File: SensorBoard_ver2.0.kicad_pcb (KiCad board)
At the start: 2 copper layers, 82.5 x 50 mm, 55 parts, among them IC1 MIC5504-3.3YM5-T5, J1 CANConn, J13 Abso, J14 Abso, J15 STLink, J16 Abso, J18 Abso, J19 Abso, J2 CANConn, J20 Enc5, J3 Enc1, J4 Enc2, J5 Enc3, J6 Enc4, SW1 CAN_Terminal, SW2 IDSetSW, SW3 Reset, SW4 IDSetSW, U1 L7805, U2 ATA6561, U4 STM32F303K8Tx, U5 MAX3485, Y1 Crystal

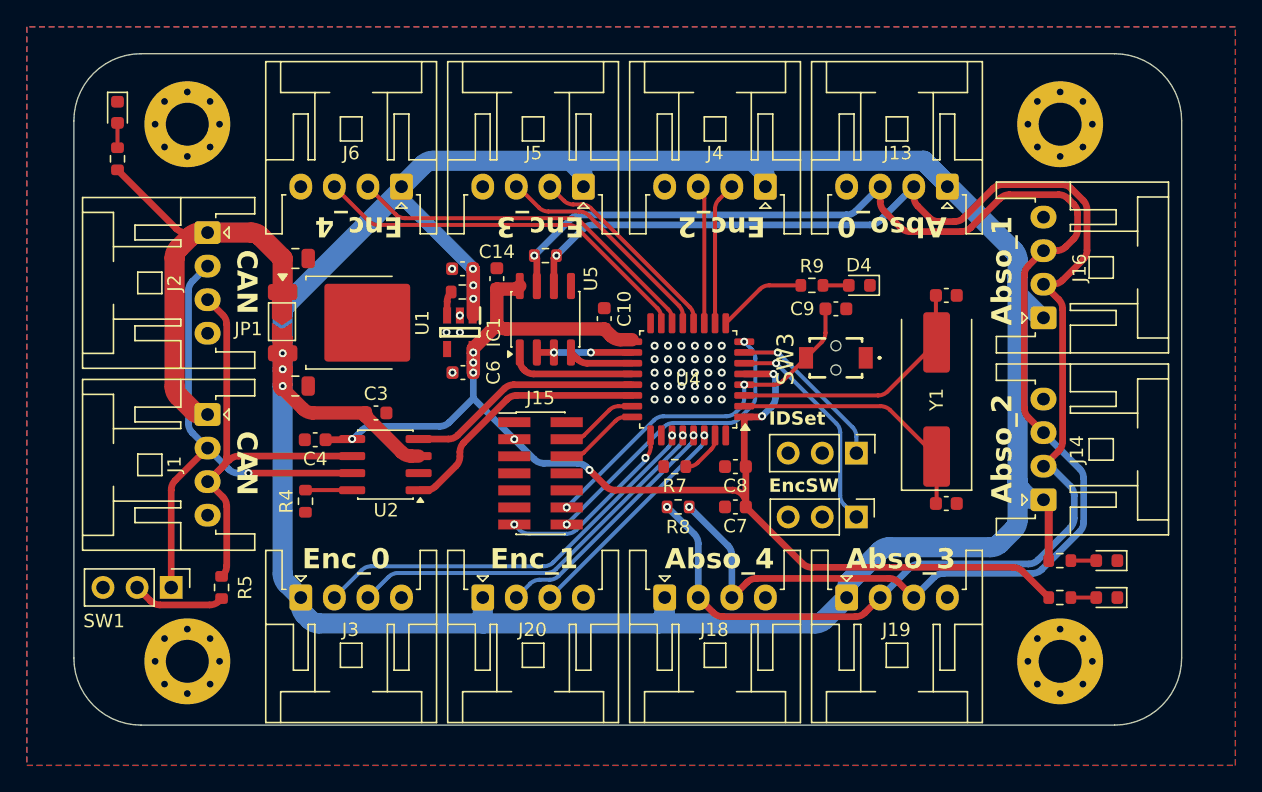
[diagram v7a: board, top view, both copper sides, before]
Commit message: ver1、完成形
なんか、いろいろ制御との兼ね合いでダメなところが出てきた…
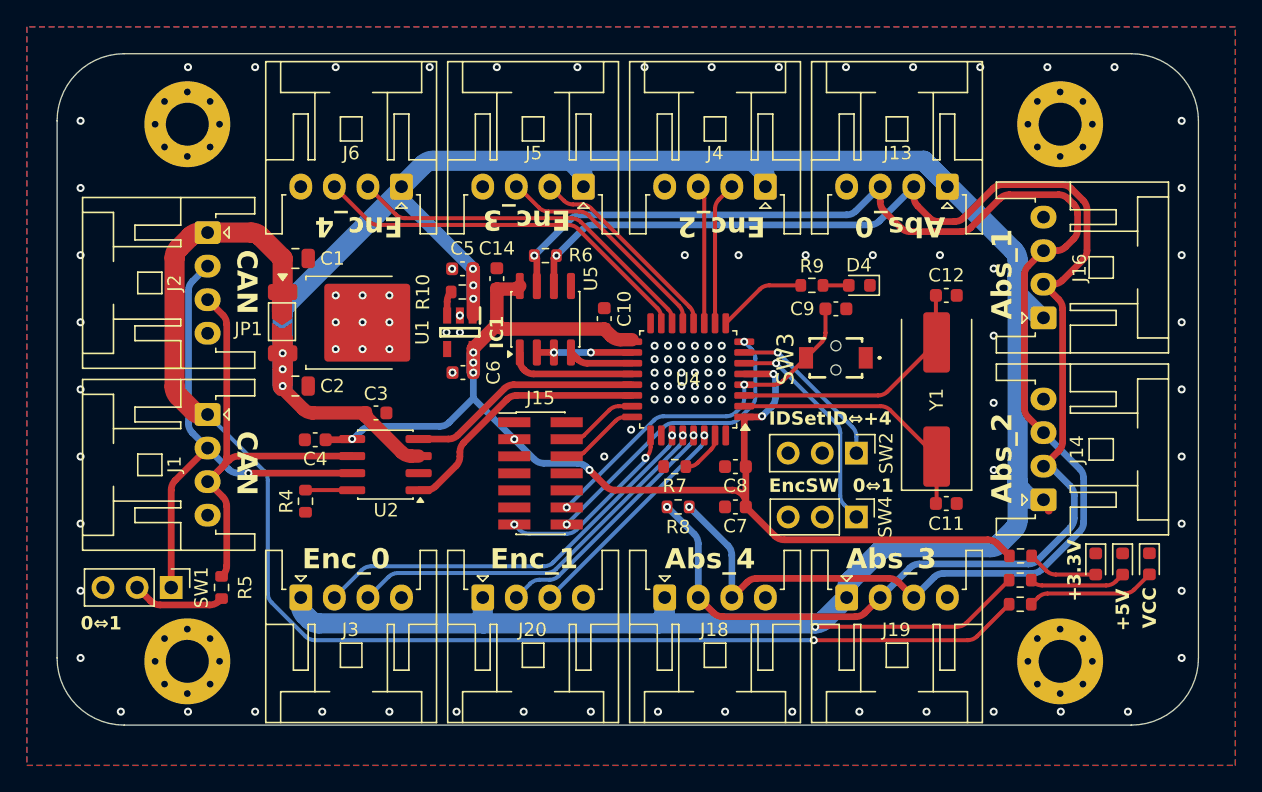
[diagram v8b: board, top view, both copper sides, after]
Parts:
- moved D1 83.9 mm to (138.6, 135.0)
- moved R1 75.0 mm to (129.0, 138.0), turned to 0 degrees
- moved R3 4.26 mm to (129.0, 134.4)
- moved R2 3.29 mm to (129.0, 136.2)
- moved D3 2.63 mm to (134.6, 135.0), turned to -90 degrees
- moved D2 1.20 mm to (136.6, 135.0), turned to -90 degrees
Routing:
- net VCC: track 35.4 -> 101.4 mm, vias 0 -> 1
- net Net-(D1-A): track 1.85 -> 9.63 mm
- net Net-(D2-A): track 1.89 -> 7.21 mm
- net +3.3V: track 97.6 -> 93.4 mm
- net +5V: track 214.3 -> 210.2 mm, vias 6 -> 7
- net Net-(D3-A): track 1.89 -> 5.30 mm
- net GND: vias 35 -> 103
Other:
- board size 82.5 x 50 mm -> 85 x 50 mm
- board text added: "+3.3V"
- board text added: "+5V"
- board text added: "0⇔1"
- board text added: "Abs_0"
- board text added: "Abs_1"
- board text added: "Abs_2"
- board text added: "Abs_3"
- board text added: "Abs_4"
- board text added: "ID⇔+4"
- board text added: "SensorBoard ver1"
- board text added: "VCC"
- board text added: "♨"
- board text added: "「Design」 Hardware:Hama Firmware:JAGA"
- board text added: "「Size」 85mm×50mm 65mm×40mm"
- board text removed: "Abso_0"
- board text removed: "Abso_1"
- board text removed: "Abso_2"
- board text removed: "Abso_3"
- board text removed: "Abso_4"
